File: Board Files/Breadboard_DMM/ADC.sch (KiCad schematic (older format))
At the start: 18 parts

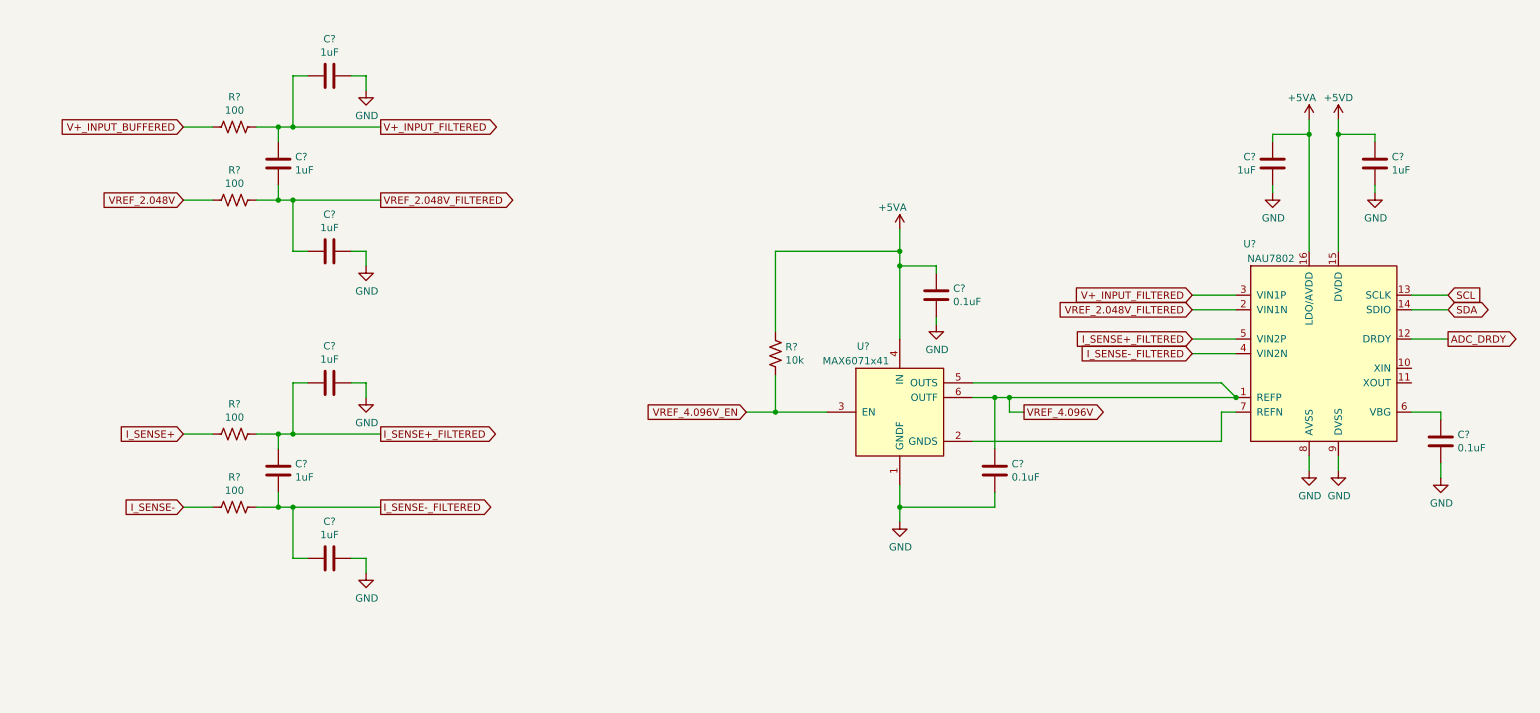
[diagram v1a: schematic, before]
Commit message: Starting converting to hierachichal design
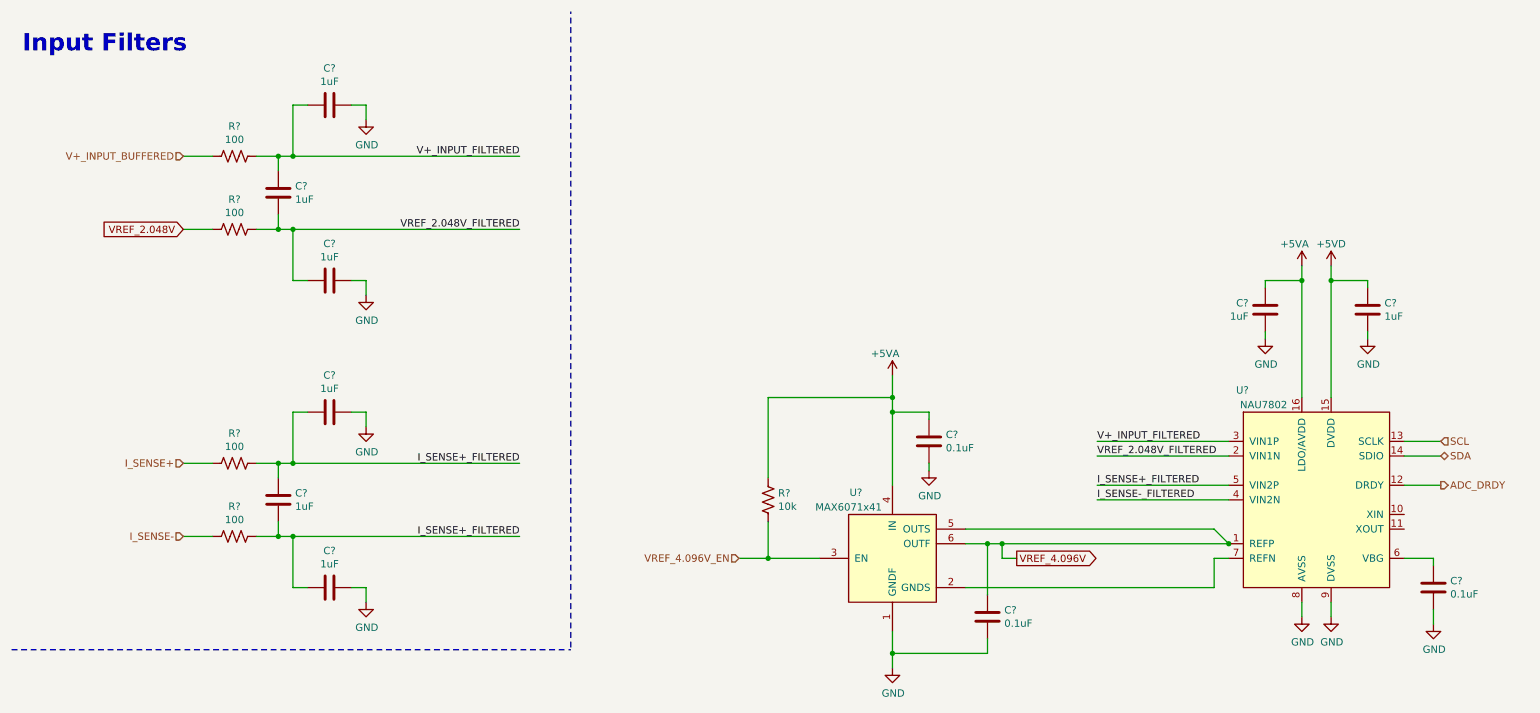
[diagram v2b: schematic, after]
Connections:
- net I_SENSE+_FILTERED: now also C?.1, C?.2, R?.2
- net I_SENSE-_FILTERED: no longer C?.1, C?.2, R?.2
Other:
- note added: "Input Filters"
- moved on the sheet: C?, R?, U?

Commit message: Finished main design, cleaning up schematic
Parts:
- added Q? (x2): NTZD3154N, Package_TO_SOT_SMD:SOT-563, symbol irex_Transistor_FET:NTZD3154N
- added R?: 10k, symbol Device:R_US
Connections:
- net +5VD: now also R?.2
- net GND: now also Q?.1 (S1), Q?.4 (S2)
- net ADC_DRDY: no longer names the net of U?.12 (DRDY)
- net ADC_DRDY: now also Q?.2 (G1)
- net VREF_4.096V_EN: no longer names the net of R?.1, U?.3 (EN)
- net VREF_4.096V_EN: now also Q?.3 (D2)
- new net ADC_~DRDY: Q?.6 (D1), R?.1
- new net VREF_4.096V_~EN: Q?.5 (G2)
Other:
- note added: "Current"
- note added: "Voltage/Ohms"
- moved on the sheet: C?, R?, U?

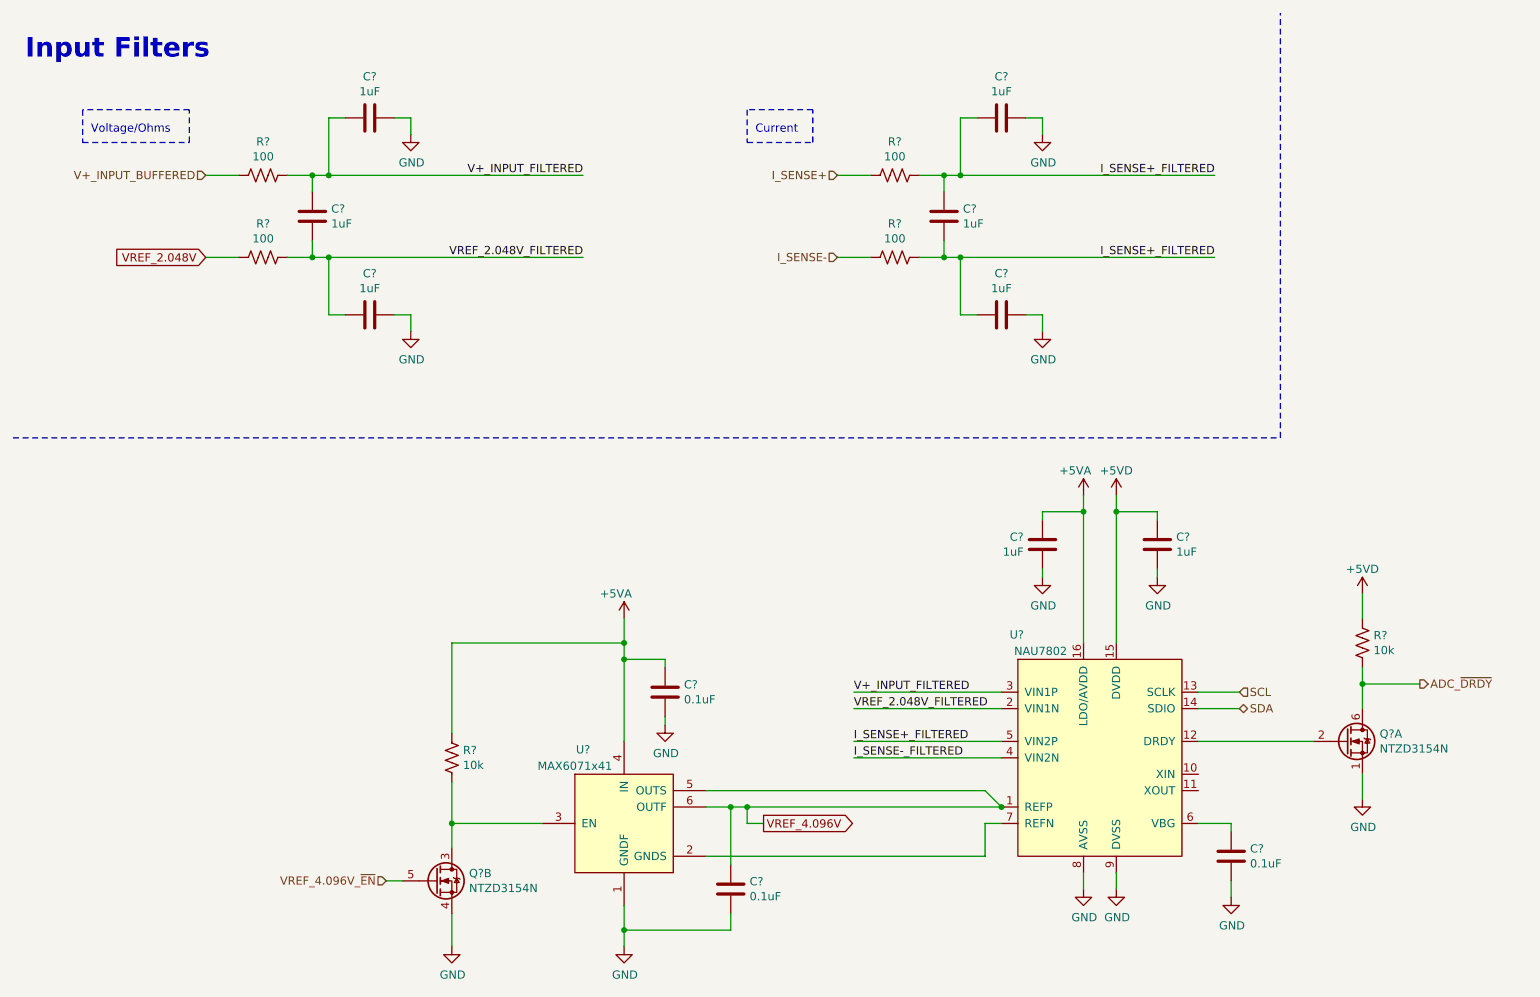
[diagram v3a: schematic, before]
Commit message: Finished main cleanup, started adding digikey part numbers
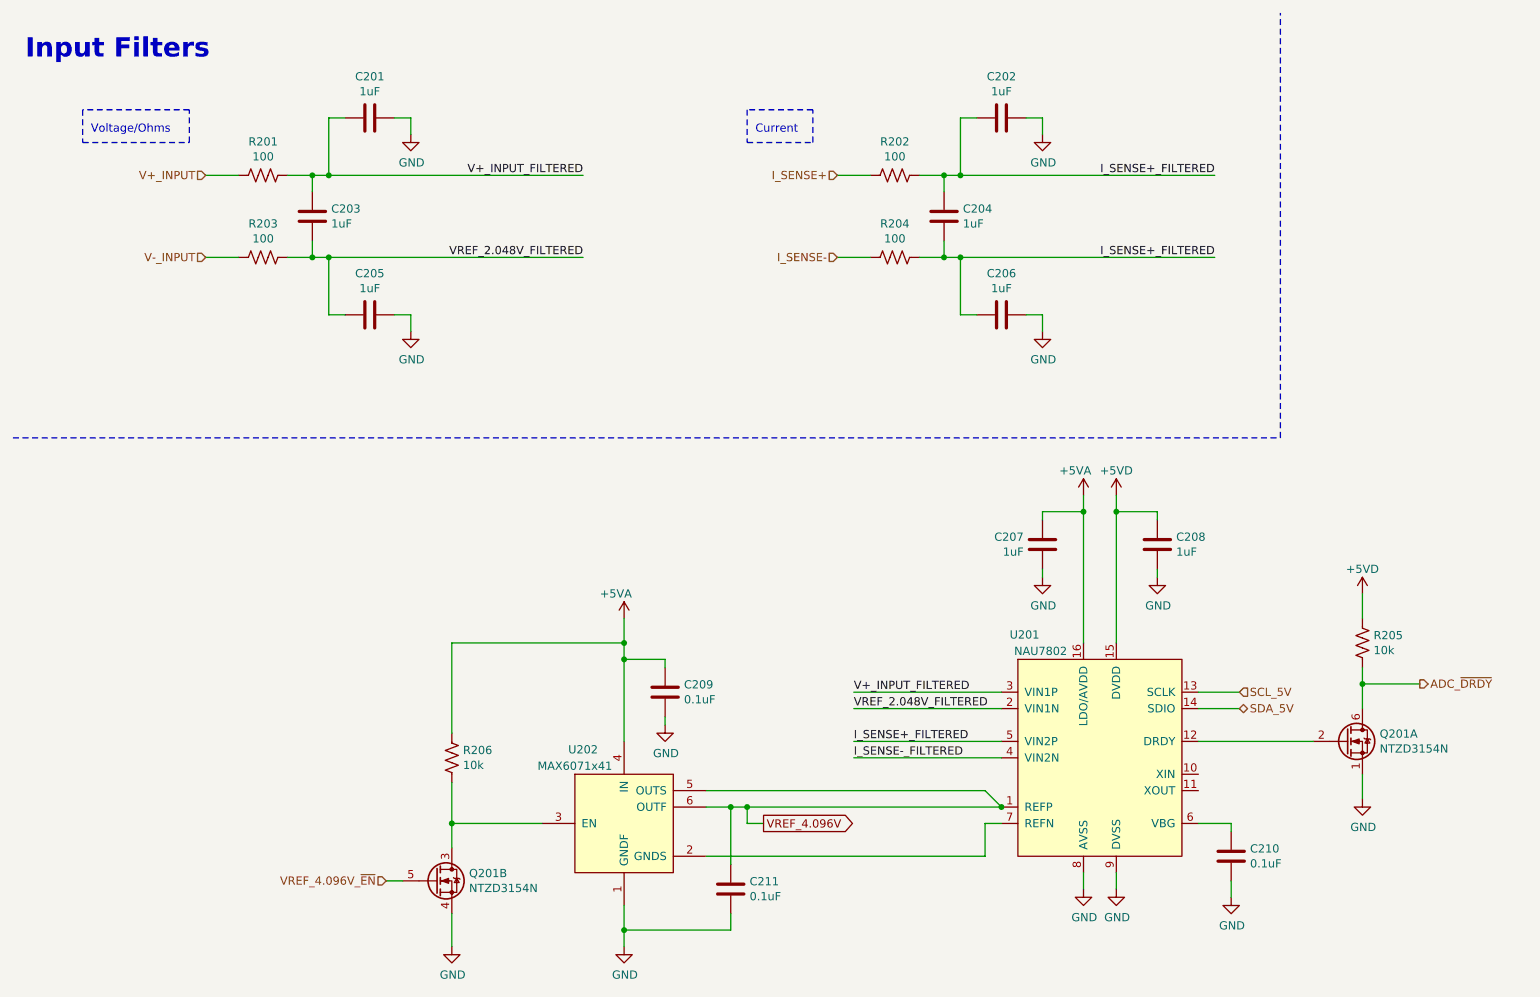
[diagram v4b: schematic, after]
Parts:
- C201, C202, C203, C204, C205, C206, C207, C208, C209, C210, C211: renamed from C?; Digi-Key PN (none) -> -
- Q201: renamed from Q?; Digi-Key PN (none) -> -
- R201, R202, R203, R204, R205, R206: renamed from R?; Digi-Key PN (none) -> -
- U201, U202: renamed from U?; Digi-Key PN (none) -> -
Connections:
- net SCL renamed SCL_5V
- net SDA renamed SDA_5V
- net V+_INPUT_BUFFERED renamed V+_INPUT
- net VREF_2.048V renamed V-_INPUT

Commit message: Started adding Digikey links
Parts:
- Q201: Digi-Key Link (none) -> https://www.digikey.com/en/products/detail/on-semiconductor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; Digi-Key PN - -> NTZD3154NT1GOSCT-ND
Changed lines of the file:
@@
 $Descr A4 11693 8268
 encoding utf-8
-Sheet 2 10
+Sheet 2 11
 Title "Toast-O-Meter"
-Date ""
+Date "2020-08-14"
 Rev "0"
 Comp ""
@@
 F 2 "Package_TO_SOT_SMD:SOT-563" H 8800 4800 50  0001 L CNN
 F 3 "https://www.onsemi.cn/PowerSolutions/document/NTZD3154N-D.PDF" H 8700 4900 50  0001 L CNN
-F 4 "" H 8700 4900 50  0001 C CNN "Digi-Key Link"
-F 5 "-" H 8700 4900 50  0001 C CNN "Digi-Key PN"
+F 4 "https://www.digikey.com/en/products/detail/on-semiconductor/NTZD3154NT1G/687137" H 8700 4900 50  0001 C CNN "Digi-Key Link"
+F 5 "NTZD3154NT1GOSCT-ND" H 8700 4900 50  0001 C CNN "Digi-Key PN"
 	1    8700 4900
 	1    0    0    -1
@@
 F 2 "Package_TO_SOT_SMD:SOT-563" H 3250 5650 50  0001 L CNN
 F 3 "https://www.onsemi.cn/PowerSolutions/document/NTZD3154N-D.PDF" H 3150 5750 50  0001 L CNN
-F 4 "" H 3150 5750 50  0001 C CNN "Digi-Key Link"
-F 5 "-" H 3150 5750 50  0001 C CNN "Digi-Key PN"
+F 4 "https://www.digikey.com/en/products/detail/on-semiconductor/NTZD3154NT1G/687137" H 3150 5750 50  0001 C CNN "Digi-Key Link"
+F 5 "NTZD3154NT1GOSCT-ND" H 3150 5750 50  0001 C CNN "Digi-Key PN"
 	2    3150 5750
 	1    0    0    -1

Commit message: Finished adding parts, cleaned up, ran ERC
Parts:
- added R206, R208: 100, Resistor_SMD:R_0603_1608Metric_Pad1.05x0.95mm_HandSolder, symbol Device:R_US
- C201, C202, C203, C204, C205, C206, C207, C208: footprint (none) -> Resistor_SMD:R_0603_1608Metric_Pad1.05x0.95mm_HandSolder; Digi-Key Link (none) -> https://www.digikey.com/en/products/detail/samsung-electro-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; Digi-Key PN - -> 1276-6524-1-ND
- C209: footprint (none) -> Resistor_SMD:R_0603_1608Metric_Pad1.05x0.95mm_HandSolder; Digi-Key Link (none) -> https://www.digikey.com/en/products/detail/samsung-electro-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; Digi-Key PN - -> 1276-1006-1-ND
- C210: renamed from C211; footprint (none) -> Resistor_SMD:R_0603_1608Metric_Pad1.05x0.95mm_HandSolder; Digi-Key Link (none) -> https://www.digikey.com/en/products/detail/samsung-electro-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; Digi-Key PN - -> 1276-1006-1-ND
- C211: renamed from C210; footprint (none) -> Resistor_SMD:R_0603_1608Metric_Pad1.05x0.95mm_HandSolder; Digi-Key Link (none) -> https://www.digikey.com/en/products/detail/samsung-electro-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; Digi-Key PN - -> 1276-1006-1-ND
- R201, R202, R203, R204: footprint (none) -> Resistor_SMD:R_0603_1608Metric_Pad1.05x0.95mm_HandSolder; Digi-Key Link (none) -> https://www.digikey.com/en/products/detail/yageo/RC0603FR-0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; Digi-Key PN - -> 311-100HRCT-ND
- R205: footprint (none) -> Resistor_SMD:R_0603_1608Metric_Pad1.05x0.95mm_HandSolder; Digi-Key Link (none) -> https://www.digikey.com/en/products/detail/yageo/RC0603FR-0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; Digi-Key PN - -> 311-10.0KHRCT-ND
- R207: renamed from R206; footprint (none) -> Resistor_SMD:R_0603_1608Metric_Pad1.05x0.95mm_HandSolder; Digi-Key Link (none) -> https://www.digikey.com/en/products/detail/yageo/RC0603FR-0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; Digi-Key PN - -> 311-10.0KHRCT-ND
- U201: Digi-Key Link (none) -> https://www.digikey.com/en/products/detail/nuvoton-technolo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; Digi-Key PN - -> NAU7802SGI-ND
- U202: Digi-Key Link (none) -> https://www.digikey.com/en/products/detail/maxim-integrated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; Digi-Key PN - -> MAX6071AAUT41+TCT-ND
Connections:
- net I_SENSE+_FILTERED: no longer C204.2, C206.1, R204.2
- net I_SENSE-_FILTERED: now also C204.2, C206.1, R204.2
- net VREF_4.096V_~EN: now also R208.1; no longer Q201.5 (G2)
- net at U201.12 (DRDY): now also R206.1; no longer Q201.2 (G1)
- new net: Q201.5 (G2), R208.2
- new net: Q201.2 (G1), R206.2
- no-connect marks 0 -> 2
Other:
- note added: "ADC & 4.096V Ref"
- moved on the sheet: C201, C202, C203, C204, C205, C206, C207, C208, C209, C210, C211, Q201A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

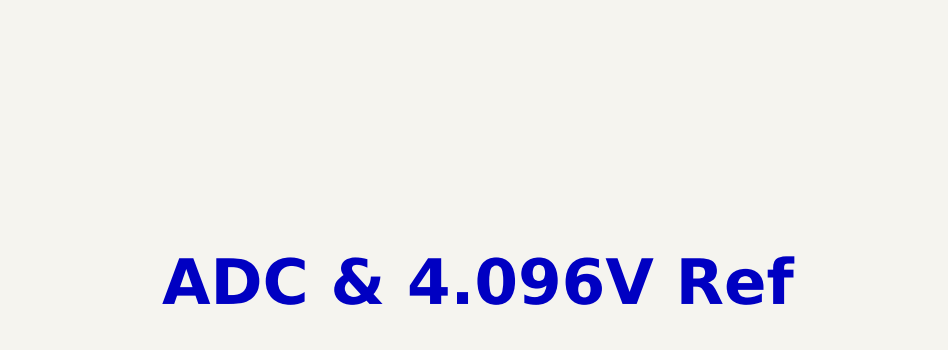
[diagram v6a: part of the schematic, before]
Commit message: Updated probe connector arrangement
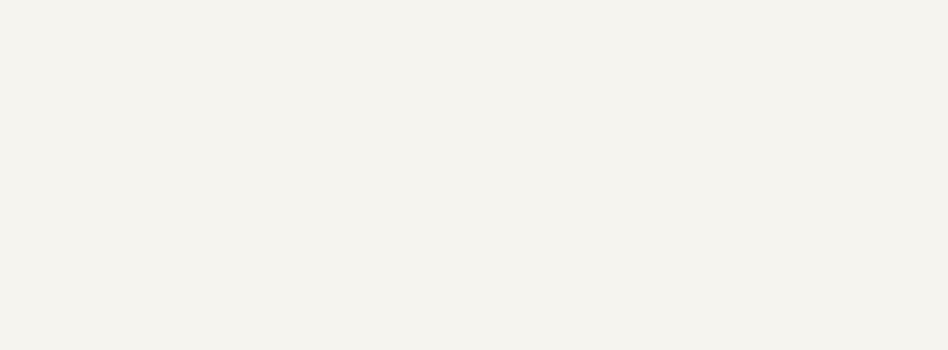
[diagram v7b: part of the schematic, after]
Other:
- note removed: "ADC & 4.096V Ref"
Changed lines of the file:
@@
 Sheet 2 8
 Title "Toast-O-Meter"
-Date "2020-08-14"
+Date "2020-10-06"
 Rev "0"
 Comp ""
-Comment1 ""
+Comment1 "Isaac Rex"
 Comment2 ""
 Comment3 ""
@@
 NoConn ~ 9250 7100
 NoConn ~ 9250 7000
-Text Notes 12400 9750 0    200  ~ 40
-ADC & 4.096V Ref
 $EndSCHEMATC
